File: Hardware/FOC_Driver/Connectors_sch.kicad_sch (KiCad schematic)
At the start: 15 parts, among them J1 USB_C_Receptacle_USB2.0_16P, J2 MR30, J4 XT30, J5 Conn_ARM_SWD_TagConnect_TC203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, J6 TestPoint, J7 TestPoint, J8 TestPoint, U2 USBLC6-2SC6

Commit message: schematic updates
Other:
- moved on the sheet: C1, C2, D1, D2, F1, J1, J2, J4, J5, J6, J7, J8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

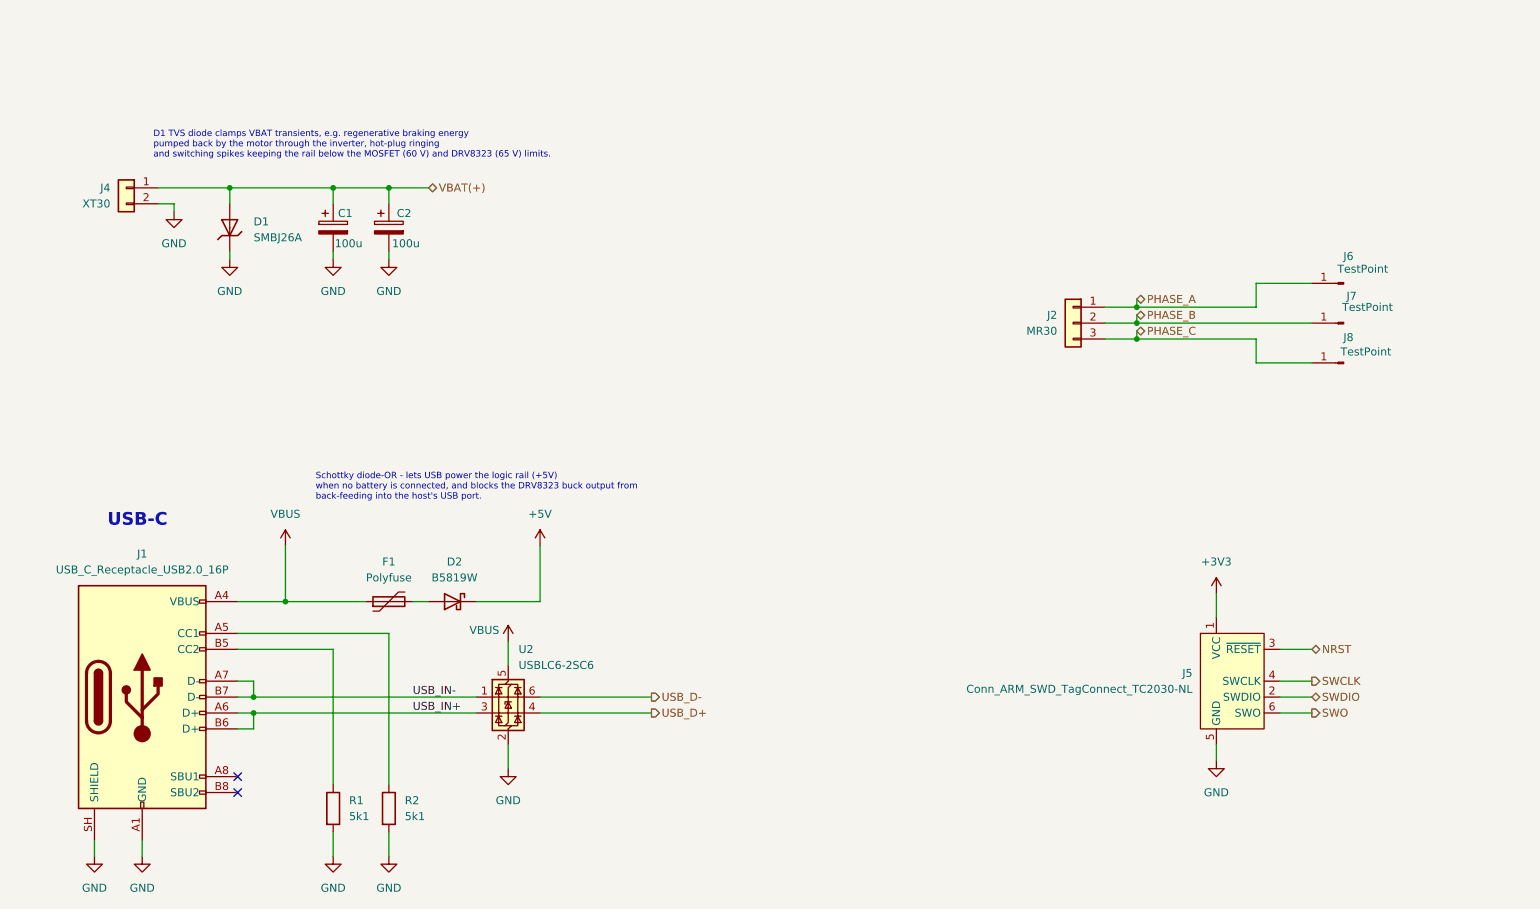
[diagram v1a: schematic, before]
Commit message: schematic completed
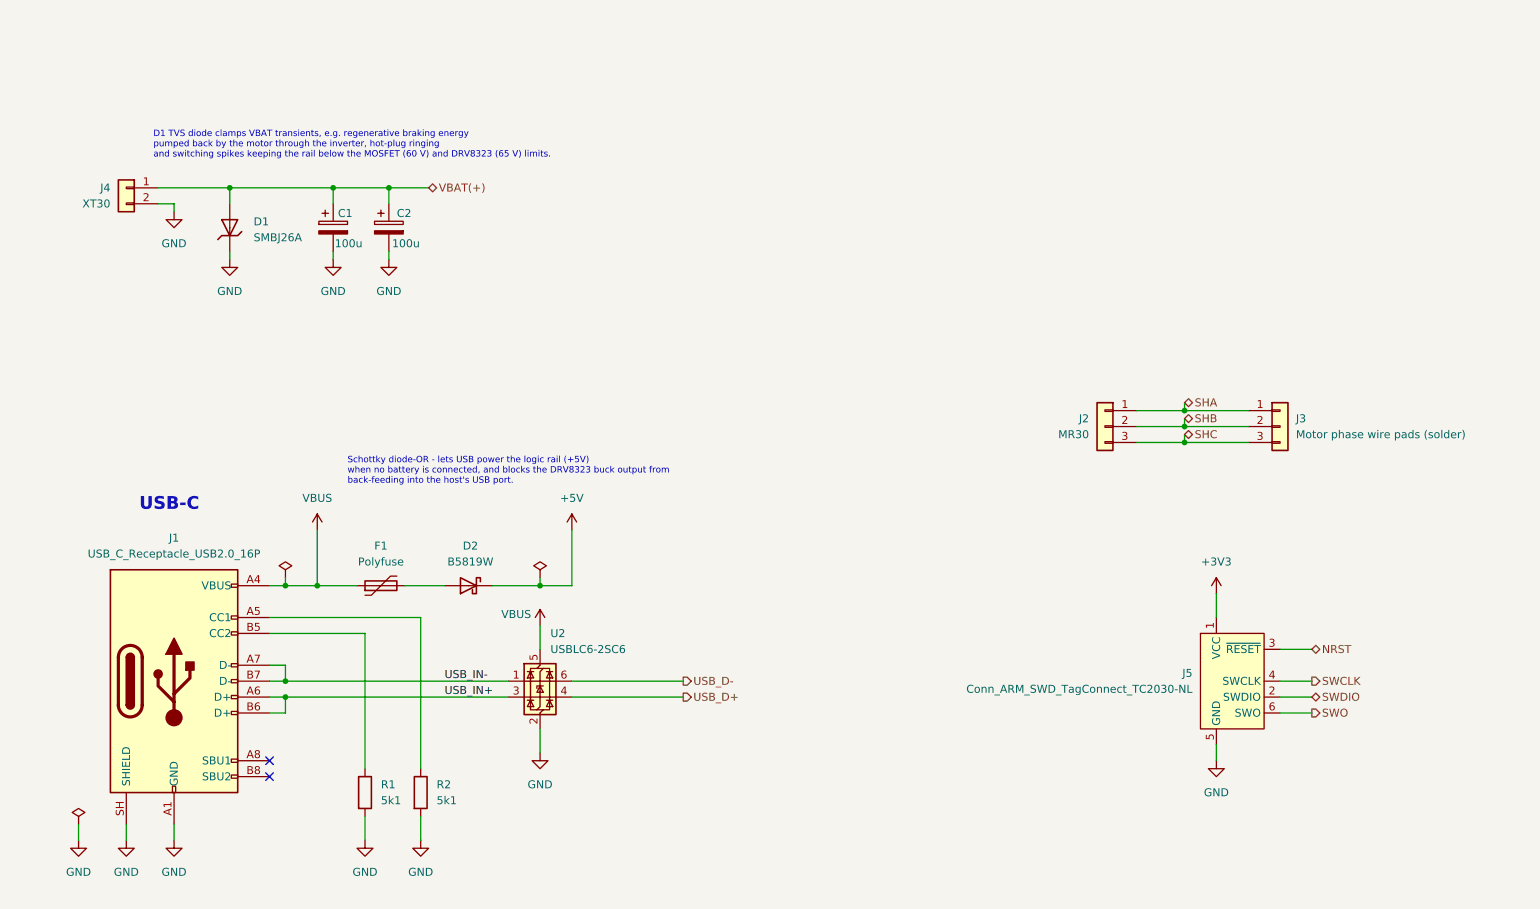
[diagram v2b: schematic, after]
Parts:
- removed J6, J7, J8: TestPoint, TestPoint:TestPoint_Loop_D1.80mm_Drill1.0mm_Beaded, symbol Connector:Conn_01x01_Pin
- added J3: Motor phase wire pads (solder), Connector_Wire:SolderWire-0.15sqmm_1x03_P4mm_D0.5mm_OD1.5mm, symbol Connector_Generic:Conn_01x03
- C1, C2: footprint (none) -> Capacitor_SMD:CP_Elec_8x10.5
- R1, R2: footprint (none) -> eResistor:R_0402_1005Metric
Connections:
- net PHASE_A renamed SHA
- net SHA: now also J3.1 (Pin_1)
- net PHASE_B renamed SHB
- net SHB: now also J3.2 (Pin_2)
- net PHASE_C renamed SHC
- net SHC: now also J3.3 (Pin_3)
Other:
- moved on the sheet: D2, F1, J1, J2, R1, R2, U2

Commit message: Schematic update, XT30/MR30 connectors and PCB layout in progress
- Connectors: AMASS XT30PW and MR30PW from Kicad_Libs (eConnector)
- Schematic updates on main, MCU and gate driver sheets
- PCB: footprints placed, routing in progress
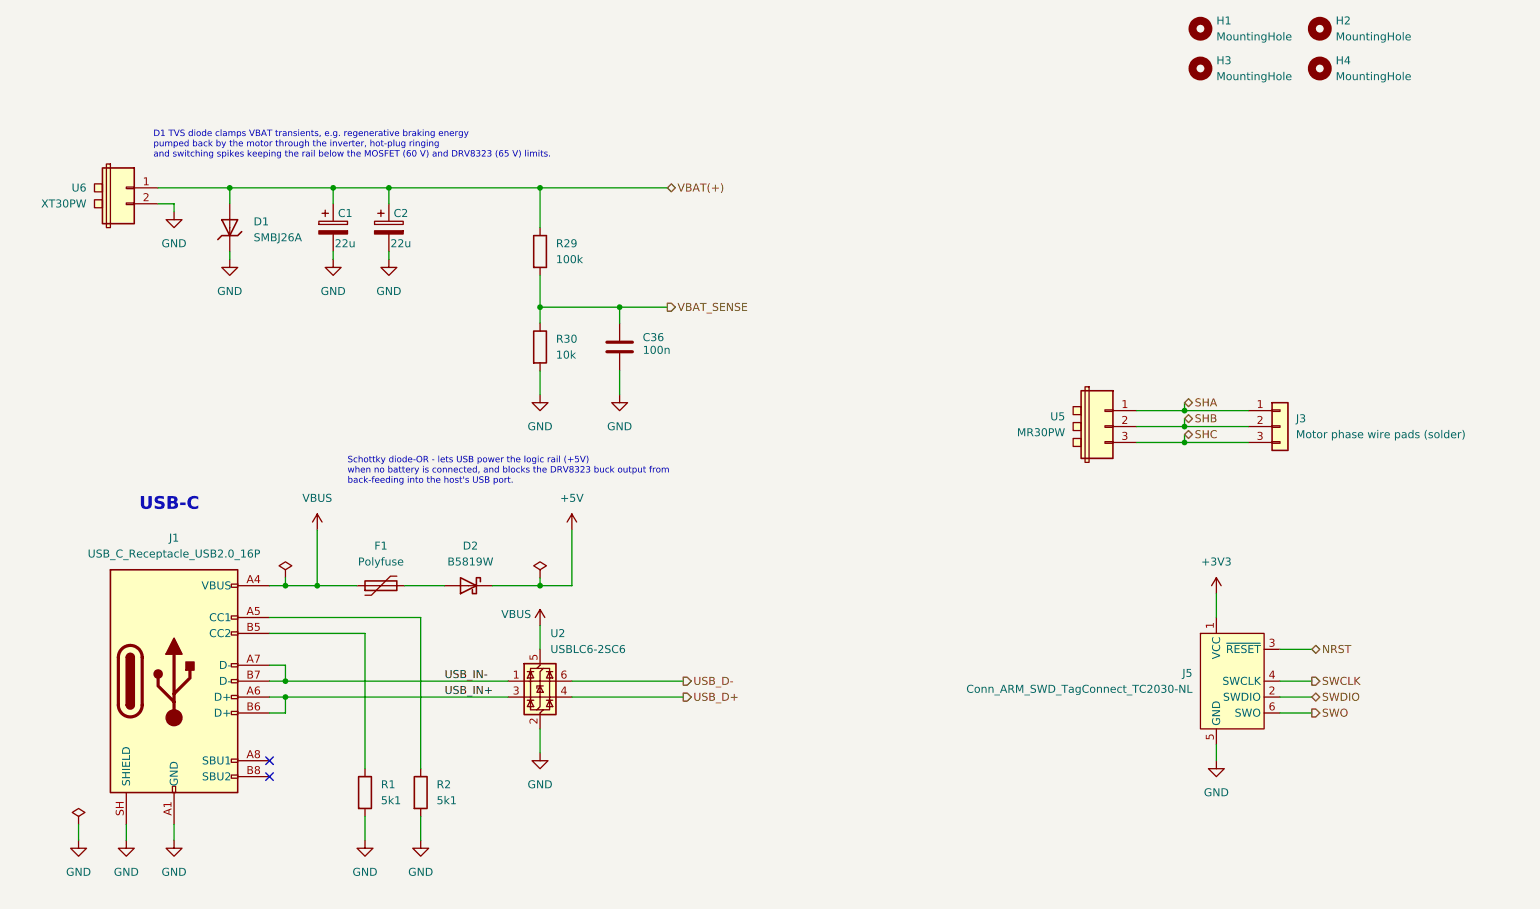
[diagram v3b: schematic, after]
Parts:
- removed J2: MR30, Connector_AMASS:AMASS_MR30PW-M_1x03_P3.50mm_Horizontal, symbol Connector_Generic:Conn_01x03
- removed J4: XT30, Connector_AMASS:AMASS_XT30PW-M_1x02_P2.50mm_Horizontal, symbol Connector_Generic:Conn_01x02
- added C36: 100n, eCapacitor:0402, symbol Device:C
- added H1, H2, H3, H4: MountingHole, MountingHole:MountingHole_2.7mm_M2.5_DIN965_Pad_TopOnly, symbol Mechanical:MountingHole
- added R29: 100k, eResistor:0603, symbol Device:R
- added R30: 10k, eResistor:0603, symbol Device:R
- added U5: MR30PW, eConnector:AMASS_MR30PW-M_1x03_P3.50mm_Horizontal, symbol eConnector:MR30PW
- added U6: XT30PW, eConnector:AMASS_XT30PW-M_1x02_P2.50mm_Horizontal, symbol eConnector:XT30PW
- C1, C2: value 100u -> 22u; footprint Capacitor_SMD:CP_Elec_8x10.5 -> Capacitor_SMD:CP_Elec_6.3x5.4
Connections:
- net GND: now also C36.1, R30.2, U6.2
- net SHA: now also U5.1
- net SHB: now also U5.2
- net SHC: now also U5.3
- net VBAT(+): now also R29.1, U6.1
- new net VBAT_SENSE: C36.2, R29.2, R30.1

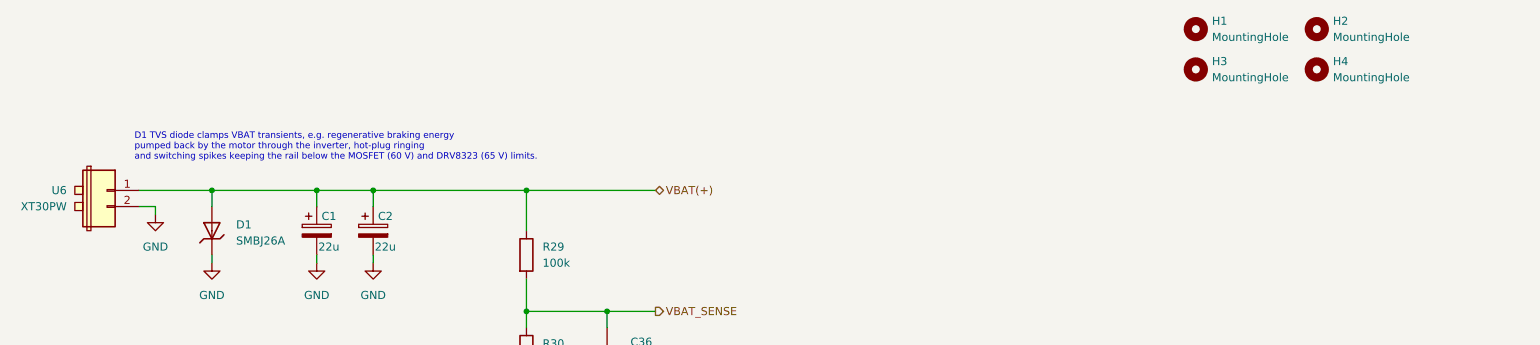
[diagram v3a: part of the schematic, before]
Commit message: Finished positioning and started layout v2
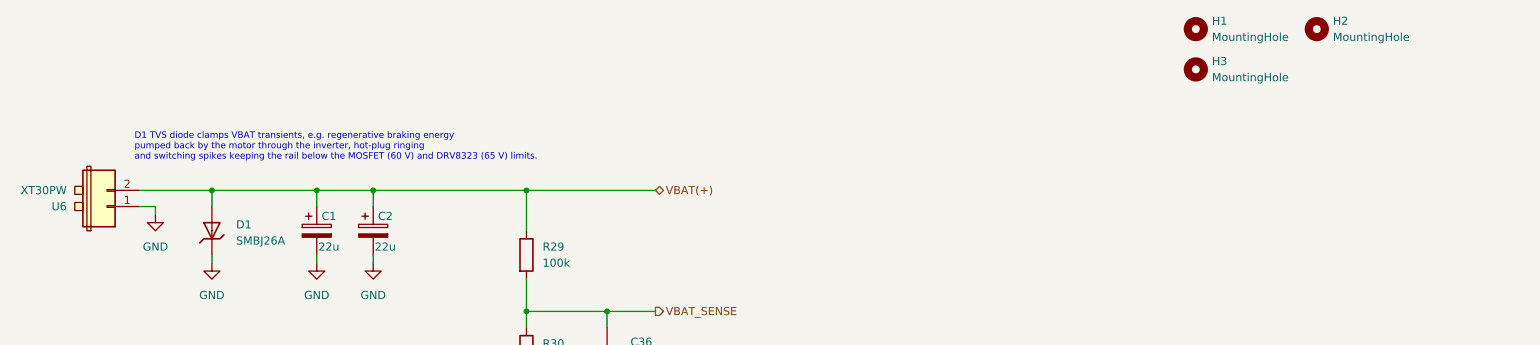
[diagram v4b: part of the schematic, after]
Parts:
- removed H4: MountingHole, MountingHole:MountingHole_2.7mm_M2.5_DIN965_Pad_TopOnly, symbol Mechanical:MountingHole
- J3: footprint Connector_Wire:SolderWire-0.15sqmm_1x03_P4mm_D0.5mm_OD1.5mm -> Connector_Wire:SolderWire-0.5sqmm_1x03_P4.6mm_D0.9mm_OD2.1mm
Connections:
- net GND: now also U6.1; no longer U6.2
- net VBAT(+): now also U6.2; no longer U6.1
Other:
- moved on the sheet: U6
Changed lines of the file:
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@@
 	)
 	(junction
+		(at 66.04 50.8)
+		(diameter 0)
+		(color 0 0 0 0)
+	)
+	(junction
 		(at 115.57 114.3)
 		(diameter 0)
@@
 	)
 	(junction
-		(at 66.04 50.8)
-		(diameter 0)
-		(color 0 0 0 0)
-	)
-	(junction
 		(at 74.93 132.08)
 		(diameter 0)
@@
 	(wire
 		(pts
-			(xy 87.63 154.94) (xy 87.63 151.13)
+			(xy 54.61 50.8) (xy 66.04 50.8)
 		)
 		(stroke
@@
 	(wire
 		(pts
-			(xy 223.52 142.24) (xy 223.52 139.7)
+			(xy 87.63 154.94) (xy 87.63 151.13)
 		)
 		(stroke
@@
 	(wire
 		(pts
-			(xy 86.36 114.3) (xy 80.01 114.3)
+			(xy 223.52 142.24) (xy 223.52 139.7)
 		)
 		(stroke
@@
 	(wire
 		(pts
-			(xy 238.76 132.08) (xy 233.68 132.08)
+			(xy 86.36 114.3) (xy 80.01 114.3)
 		)
 		(stroke
@@
 	(wire
 		(pts
-			(xy 57.15 53.34) (xy 54.61 53.34)
+			(xy 238.76 132.08) (xy 233.68 132.08)
 		)
 		(stroke
@@
 	(wire
 		(pts
+			(xy 54.61 53.34) (xy 57.15 53.34)
+		)
+		(stroke
+			(width 0)
+			(type default)
+		)
+	)
+	(wire
+		(pts
 			(xy 223.52 115.57) (xy 223.52 119.38)
 		)
@@
 	(wire
 		(pts
-			(xy 66.04 50.8) (xy 54.61 50.8)
-		)
-		(stroke
-			(width 0)
-			(type default)
-		)
-	)
-	(wire
-		(pts
 			(xy 66.04 62.23) (xy 66.04 60.96)
 		)
@@
 	(symbol
 		(lib_id "eConnector:XT30PW")
-		(at 48.26 50.8 0)
-		(mirror y)
+		(at 48.26 53.34 180)
 		(unit 1)
 		(body_style 1)
@@
 		(dnp no)
 		(property "Reference" "U6"
-			(at 43.18 50.7999 0)
+			(at 43.18 53.3401 0)
 			(show_name no)
 			(do_not_autoplace no)
@@
 		)
 		(property "Value" "XT30PW"
-			(at 43.18 53.3399 0)
+			(at 43.18 50.8001 0)
 			(show_name no)
 			(do_not_autoplace no)
@@
 		)
 		(property "Footprint" "eConnector:AMASS_XT30PW-M_1x02_P2.50mm_Horizontal"
-			(at 48.26 50.8 0)
+			(at 48.26 53.34 0)
 			(hide yes)
 			(show_name no)
@@
 		)
 		(property "Datasheet" "${KIPRJMOD}/../KiCad_Libs/eConnector/datasheet/XT30PW-M.pdf"
-			(at 48.26 41.402 0)
+			(at 48.26 62.738 0)
 			(hide yes)
 			(show_name no)
@@
 		)
 		(property "Description" ""
-			(at 48.26 50.8 0)
+			(at 48.26 53.34 0)
 			(hide yes)
 			(show_name no)
@@
 	)
 	(symbol
-		(lib_id "Mechanical:MountingHole")
-		(at 240.03 31.75 0)
-		(unit 1)
-		(body_style 1)
-		(exclude_from_sim no)
-		(in_bom no)
-		(on_board yes)
-		(in_pos_files yes)
-		(dnp no)
-		(fields_autoplaced yes)
-		(property "Reference" "H4"
-			(at 242.57 30.4799 0)
-			(show_name no)
-			(do_not_autoplace no)
-			(effects
-				(font
-					(size 1.27 1.27)
-				)
-				(justify left)
-			)
-		)
-		(property "Value" "MountingHole"
-			(at 242.57 33.0199 0)
-			(show_name no)
-			(do_not_autoplace no)
-			(effects
-				(font
-					(size 1.27 1.27)
-				)
-				(justify left)
-			)
-		)
-		(property "Footprint" "MountingHole:MountingHole_2.7mm_M2.5_DIN965_Pad_TopOnly"
-			(at 240.03 31.75 0)
-			(hide yes)
-			(show_name no)
-			(do_not_autoplace no)
-			(effects
-				(font
-					(size 1.27 1.27)
-				)
-			)
-		)
-		(property "Datasheet" ""
-			(at 240.03 31.75 0)
-			(hide yes)
-			(show_name no)
-			(do_not_autoplace no)
-			(effects
-				(font
-					(size 1.27 1.27)
-				)
-			)
-		)
-		(property "Description" "Mounting Hole without connection"
-			(at 240.03 31.75 0)
-			(hide yes)
-			(show_name no)
-			(do_not_autoplace no)
-			(effects
-				(font
-					(size 1.27 1.27)
-				)
-			)
-		)
-		(instances
-			(project "FOC_Driver"
-				(path "/56350f0b-fa2d-4452-8705-62cde497823d/eb2fd16c-c824-42dc-a584-a92c0d277782"
-					(reference "H4")
-					(unit 1)
-				)
-			)
-		)
-	)
-	(symbol
 		(lib_id "eConnector:MR30PW")
 		(at 205.74 86.36 0)
@@
 			)
 		)
-		(property "Footprint" "Connector_Wire:SolderWire-0.15sqmm_1x03_P4mm_D0.5mm_OD1.5mm"
+		(property "Footprint" "Connector_Wire:SolderWire-0.5sqmm_1x03_P4.6mm_D0.9mm_OD2.1mm"
 			(at 233.68 88.9 0)
 			(hide yes)
